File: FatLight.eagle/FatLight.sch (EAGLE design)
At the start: 26 parts, among them J1 12V, Q1 IRF540, Q2 IRF540, Q3 IRF540, Q4 16MHz, U1 ATMEGA328P-PU

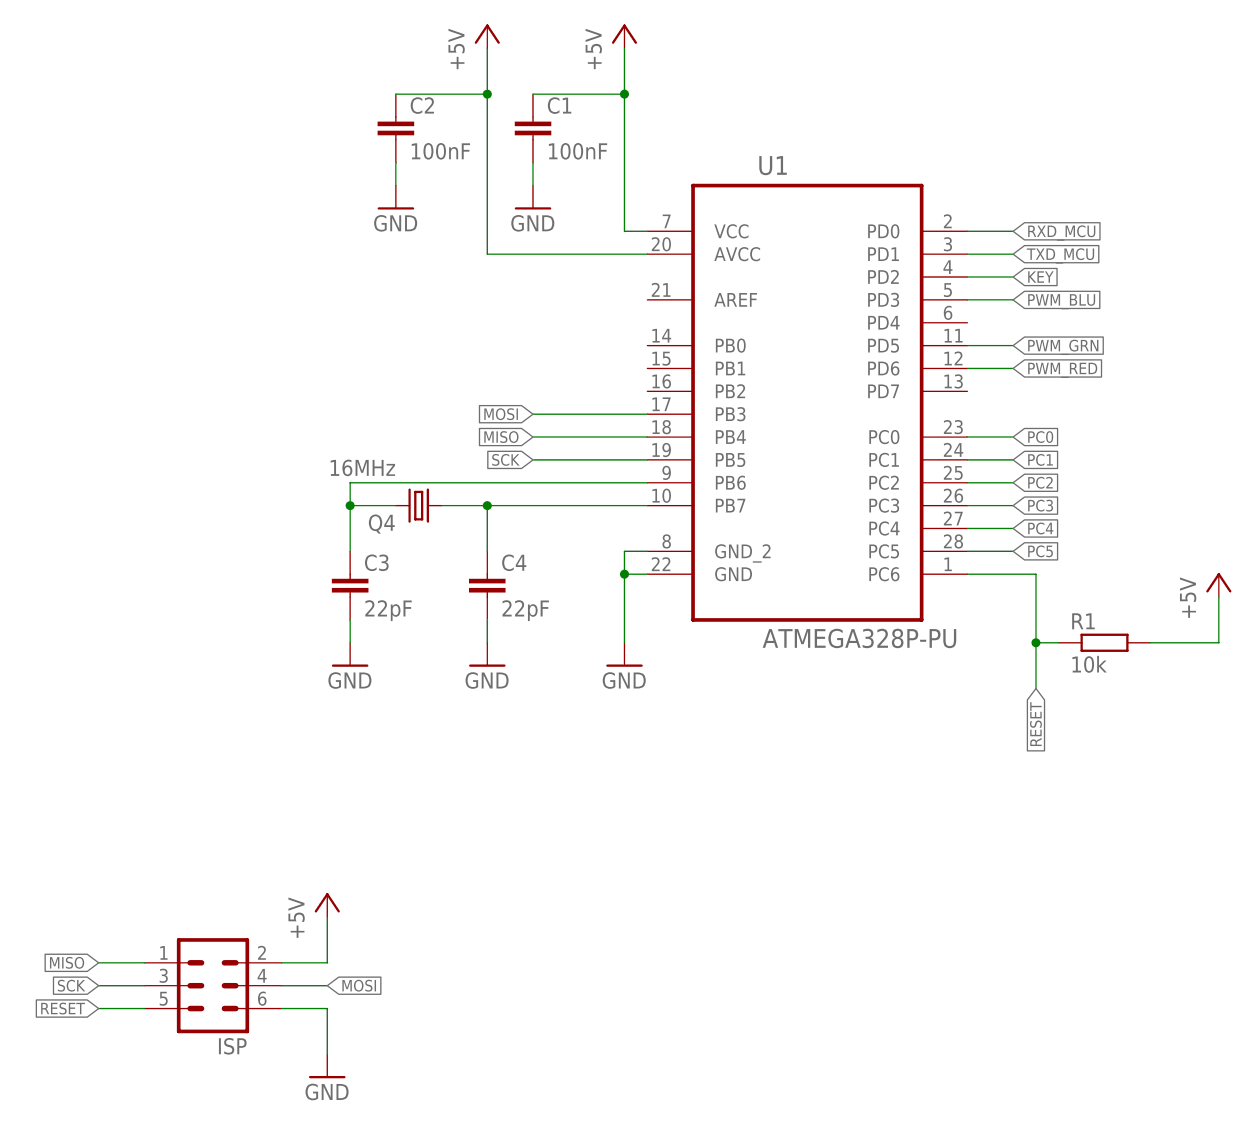
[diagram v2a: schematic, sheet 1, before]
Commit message: Implemented Bluetooth control
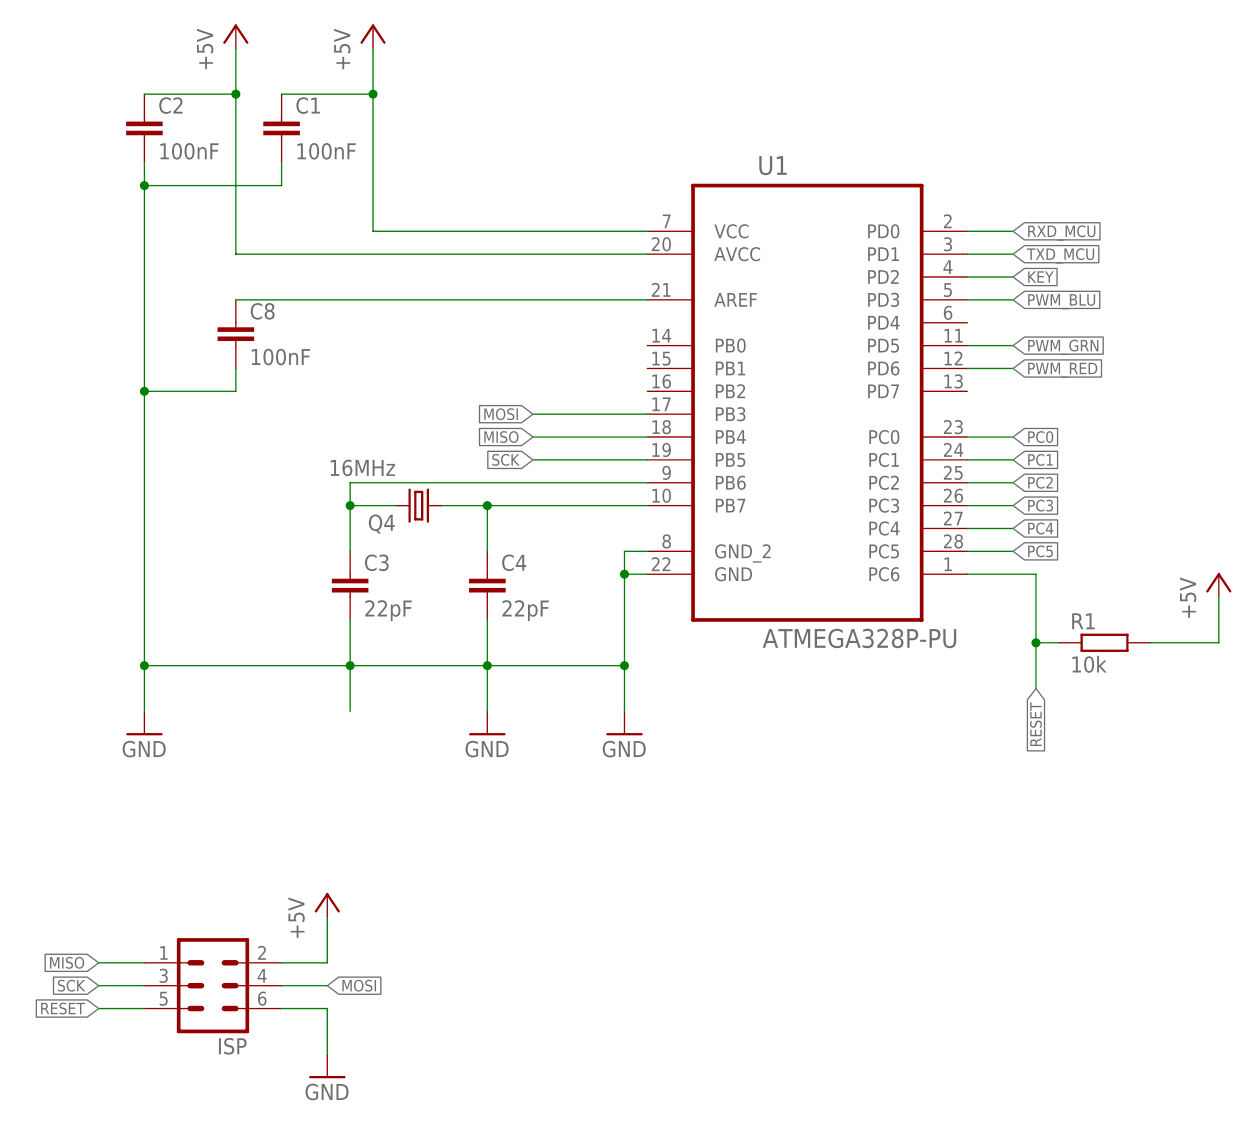
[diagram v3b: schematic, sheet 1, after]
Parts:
- added C8: 100nF, rcl:C-EU025-025X050
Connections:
- new net N$5: C8.1, U1.AREF
- net GND: now also C8.2
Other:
- moved on the sheet: C1, C2
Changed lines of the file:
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@@
 <part name="R3" library="rcl" deviceset="R-EU_" device="0207/7" value="10k"/>
 <part name="R4" library="rcl" deviceset="R-EU_" device="0207/7" value="10k"/>
-<part name="GND1" library="supply1" deviceset="GND" device=""/>
 <part name="GND2" library="supply1" deviceset="GND" device=""/>
 <part name="GND3" library="supply1" deviceset="GND" device=""/>
 <part name="GND4" library="supply1" deviceset="GND" device=""/>
-<part name="GND5" library="supply1" deviceset="GND" device=""/>
 <part name="P+1" library="supply1" deviceset="+5V" device=""/>
 <part name="P+2" library="supply1" deviceset="+5V" device=""/>
@@
 <part name="GND12" library="supply1" deviceset="GND" device=""/>
 <part name="C7" library="rcl" deviceset="CPOL-EU" device="E2.5-5" value="100µF"/>
+<part name="C8" library="rcl" deviceset="C-EU" device="025-025X050" value="100nF"/>
 </parts>
 <sheets>
@@
 <attribute name="VALUE" x="83.82" y="91.44" size="1.778" layer="96" rot="R180"/>
 </instance>
-<instance part="C1" gate="G$1" x="99.06" y="129.54"/>
-<instance part="C2" gate="G$1" x="83.82" y="129.54"/>
+<instance part="C1" gate="G$1" x="71.12" y="129.54"/>
+<instance part="C2" gate="G$1" x="55.88" y="129.54"/>
 <instance part="C3" gate="G$1" x="78.74" y="78.74"/>
 <instance part="C4" gate="G$1" x="93.98" y="78.74"/>
 <instance part="R1" gate="G$1" x="162.56" y="71.12"/>
-<instance part="GND1" gate="1" x="78.74" y="68.58"/>
-<instance part="GND2" gate="1" x="93.98" y="68.58"/>
-<instance part="GND3" gate="1" x="109.22" y="68.58"/>
-<instance part="GND4" gate="1" x="83.82" y="119.38"/>
-<instance part="GND5" gate="1" x="99.06" y="119.38"/>
-<instance part="P+1" gate="1" x="93.98" y="139.7"/>
-<instance part="P+2" gate="1" x="109.22" y="139.7"/>
+<instance part="GND2" gate="1" x="93.98" y="60.96"/>
+<instance part="GND3" gate="1" x="109.22" y="60.96"/>
+<instance part="GND4" gate="1" x="55.88" y="60.96"/>
+<instance part="P+1" gate="1" x="66.04" y="139.7"/>
+<instance part="P+2" gate="1" x="81.28" y="139.7"/>
 <instance part="P+3" gate="1" x="175.26" y="78.74"/>
 <instance part="FRAME1" gate="G$1" x="0" y="0"/>
@@
 <instance part="GND9" gate="1" x="76.2" y="22.86"/>
 <instance part="P+7" gate="1" x="76.2" y="43.18"/>
+<instance part="C8" gate="G$1" x="66.04" y="106.68"/>
 </instances>
 <busses>
@@
 <segment>
 <pinref part="C3" gate="G$1" pin="2"/>
-<pinref part="GND1" gate="1" pin="GND"/>
-<wire x1="78.74" y1="73.66" x2="78.74" y2="71.12" width="0.1524" layer="91"/>
-</segment>
-<segment>
-<pinref part="C4" gate="G$1" pin="2"/>
-<pinref part="GND2" gate="1" pin="GND"/>
-<wire x1="93.98" y1="73.66" x2="93.98" y2="71.12" width="0.1524" layer="91"/>
-</segment>
-<segment>
+<wire x1="78.74" y1="73.66" x2="78.74" y2="68.58" width="0.1524" layer="91"/>
 <pinref part="U1" gate="A" pin="GND_2"/>
 <pinref part="GND3" gate="1" pin="GND"/>
+<wire x1="78.74" y1="68.58" x2="78.74" y2="63.5" width="0.1524" layer="91"/>
 <wire x1="111.76" y1="81.28" x2="109.22" y2="81.28" width="0.1524" layer="91"/>
 <wire x1="109.22" y1="81.28" x2="109.22" y2="78.74" width="0.1524" layer="91"/>
 <pinref part="U1" gate="A" pin="GND"/>
-<wire x1="109.22" y1="78.74" x2="109.22" y2="71.12" width="0.1524" layer="91"/>
+<wire x1="109.22" y1="78.74" x2="109.22" y2="68.58" width="0.1524" layer="91"/>
+<wire x1="109.22" y1="68.58" x2="109.22" y2="63.5" width="0.1524" layer="91"/>
 <wire x1="111.76" y1="78.74" x2="109.22" y2="78.74" width="0.1524" layer="91"/>
 <junction x="109.22" y="78.74"/>
-</segment>
-<segment>
+<pinref part="C4" gate="G$1" pin="2"/>
+<pinref part="GND2" gate="1" pin="GND"/>
+<wire x1="93.98" y1="73.66" x2="93.98" y2="68.58" width="0.1524" layer="91"/>
+<wire x1="93.98" y1="68.58" x2="93.98" y2="63.5" width="0.1524" layer="91"/>
+<wire x1="109.22" y1="68.58" x2="93.98" y2="68.58" width="0.1524" layer="91"/>
+<junction x="109.22" y="68.58"/>
+<junction x="93.98" y="68.58"/>
+<wire x1="78.74" y1="68.58" x2="93.98" y2="68.58" width="0.1524" layer="91"/>
+<junction x="78.74" y="68.58"/>
 <pinref part="C2" gate="G$1" pin="2"/>
 <pinref part="GND4" gate="1" pin="GND"/>
-<wire x1="83.82" y1="124.46" x2="83.82" y2="121.92" width="0.1524" layer="91"/>
-</segment>
-<segment>
+<wire x1="55.88" y1="124.46" x2="55.88" y2="121.92" width="0.1524" layer="91"/>
 <pinref part="C1" gate="G$1" pin="2"/>
-<pinref part="GND5" gate="1" pin="GND"/>
-<wire x1="99.06" y1="124.46" x2="99.06" y2="121.92" width="0.1524" layer="91"/>
+<wire x1="55.88" y1="121.92" x2="55.88" y2="99.06" width="0.1524" layer="91"/>
+<wire x1="55.88" y1="99.06" x2="55.88" y2="68.58" width="0.1524" layer="91"/>
+<wire x1="55.88" y1="68.58" x2="55.88" y2="63.5" width="0.1524" layer="91"/>
+<wire x1="71.12" y1="124.46" x2="71.12" y2="121.92" width="0.1524" layer="91"/>
+<wire x1="71.12" y1="121.92" x2="55.88" y2="121.92" width="0.1524" layer="91"/>
+<junction x="55.88" y="121.92"/>
+<pinref part="C8" gate="G$1" pin="2"/>
+<wire x1="66.04" y1="101.6" x2="66.04" y2="99.06" width="0.1524" layer="91"/>
+<wire x1="66.04" y1="99.06" x2="55.88" y2="99.06" width="0.1524" layer="91"/>
+<junction x="55.88" y="99.06"/>
+<wire x1="78.74" y1="68.58" x2="55.88" y2="68.58" width="0.1524" layer="91"/>
+<junction x="55.88" y="68.58"/>
 </segment>
 <segment>
@@
 <segment>
 <pinref part="U1" gate="A" pin="AVCC"/>
-<wire x1="111.76" y1="114.3" x2="93.98" y2="114.3" width="0.1524" layer="91"/>
-<wire x1="93.98" y1="114.3" x2="93.98" y2="132.08" width="0.1524" layer="91"/>
+<wire x1="111.76" y1="114.3" x2="66.04" y2="114.3" width="0.1524" layer="91"/>
+<wire x1="66.04" y1="114.3" x2="66.04" y2="132.08" width="0.1524" layer="91"/>
 <pinref part="C2" gate="G$1" pin="1"/>
-<wire x1="93.98" y1="132.08" x2="93.98" y2="137.16" width="0.1524" layer="91"/>
-<wire x1="83.82" y1="132.08" x2="93.98" y2="132.08" width="0.1524" layer="91"/>
-<junction x="93.98" y="132.08"/>
+<wire x1="66.04" y1="132.08" x2="66.04" y2="137.16" width="0.1524" layer="91"/>
+<wire x1="55.88" y1="132.08" x2="66.04" y2="132.08" width="0.1524" layer="91"/>
+<junction x="66.04" y="132.08"/>
 <pinref part="P+1" gate="1" pin="+5V"/>
 </segment>
 <segment>
 <pinref part="U1" gate="A" pin="VCC"/>
-<wire x1="111.76" y1="116.84" x2="109.22" y2="116.84" width="0.1524" layer="91"/>
-<wire x1="109.22" y1="116.84" x2="109.22" y2="132.08" width="0.1524" layer="91"/>
+<wire x1="111.76" y1="116.84" x2="81.28" y2="116.84" width="0.1524" layer="91"/>
+<wire x1="81.28" y1="116.84" x2="81.28" y2="132.08" width="0.1524" layer="91"/>
 <pinref part="C1" gate="G$1" pin="1"/>
-<wire x1="109.22" y1="132.08" x2="109.22" y2="137.16" width="0.1524" layer="91"/>
-<wire x1="99.06" y1="132.08" x2="109.22" y2="132.08" width="0.1524" layer="91"/>
-<junction x="109.22" y="132.08"/>
+<wire x1="81.28" y1="132.08" x2="81.28" y2="137.16" width="0.1524" layer="91"/>
+<wire x1="71.12" y1="132.08" x2="81.28" y2="132.08" width="0.1524" layer="91"/>
+<junction x="81.28" y="132.08"/>
 <pinref part="P+2" gate="1" pin="+5V"/>
 </segment>
@@
 </segment>
 </net>
+<net name="N$5" class="0">
+<segment>
+<pinref part="U1" gate="A" pin="AREF"/>
+<pinref part="C8" gate="G$1" pin="1"/>
+<wire x1="111.76" y1="109.22" x2="66.04" y2="109.22" width="0.1524" layer="91"/>
+</segment>
+</net>

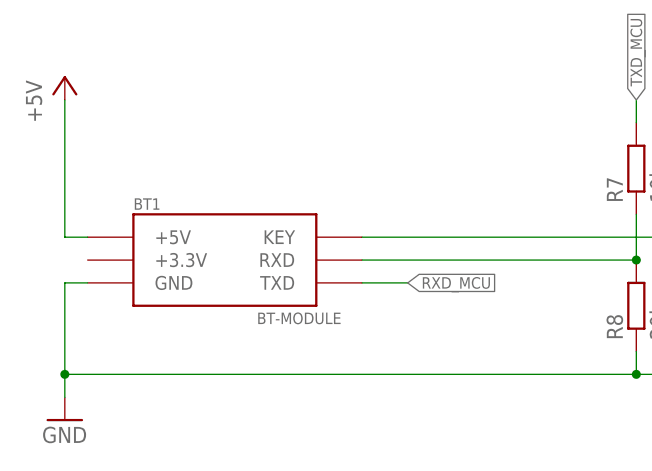
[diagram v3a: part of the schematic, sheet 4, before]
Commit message: Updated Board and Schmeatics so either of two different HC-05 module types can be fitted. Bugfixes.
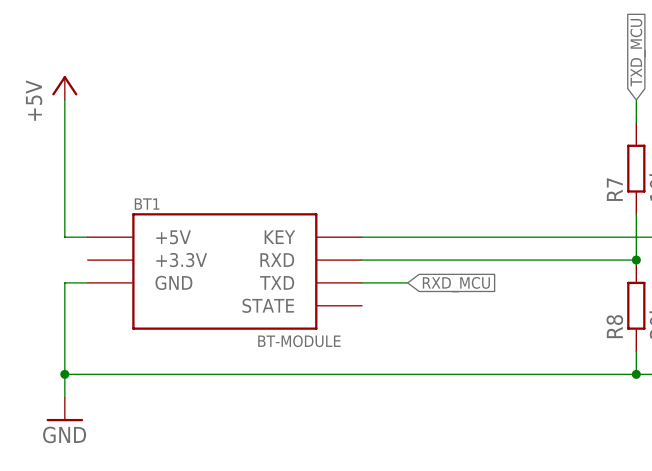
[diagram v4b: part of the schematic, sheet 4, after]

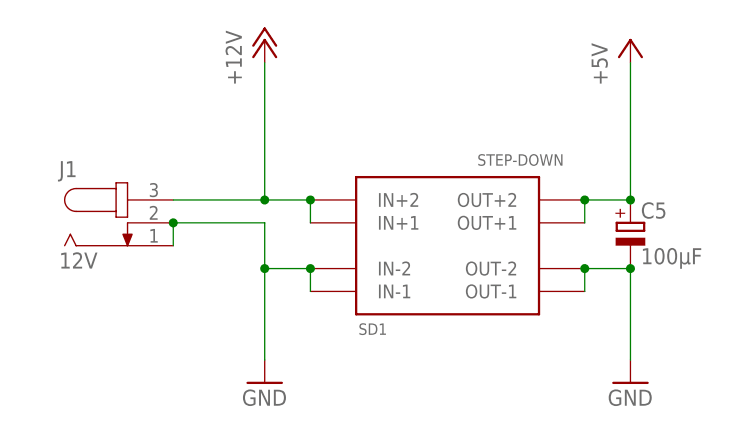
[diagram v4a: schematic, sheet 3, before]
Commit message: Fixed the dimensions of the d-sun step-down module.
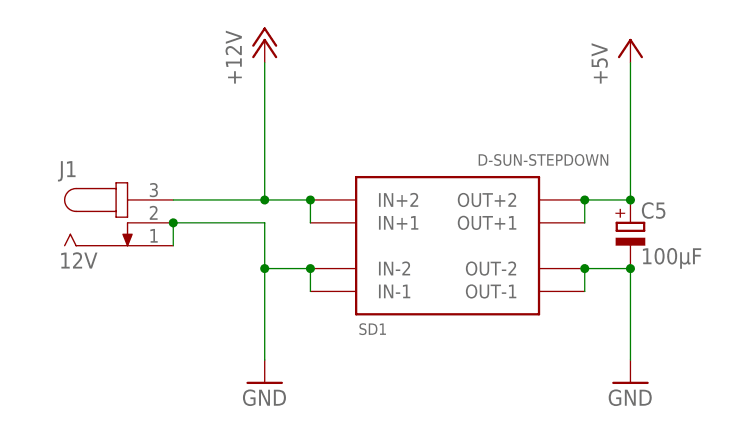
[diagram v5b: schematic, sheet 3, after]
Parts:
- SD1: value STEP-DOWN -> D-SUN-STEPDOWN; device Zap-Powerconverters:STEP-DOWN -> Zap-Powerconverters:D-SUN-STEPDOWN
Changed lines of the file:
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@@
 <part name="P+4" library="supply1" deviceset="+12V" device=""/>
 <part name="FRAME3" library="frames" deviceset="A4L-LOC" device="" value="Power"/>
-<part name="SD1" library="Zap-Powerconverters" deviceset="STEP-DOWN" device=""/>
+<part name="SD1" library="Zap-Powerconverters" deviceset="D-SUN-STEPDOWN" device=""/>
 <part name="J1" library="con-jack" deviceset="JACK-PLUG" device="0" value="12V"/>
 <part name="C5" library="rcl" deviceset="CPOL-EU" device="E2.5-5" value="100µF"/>
